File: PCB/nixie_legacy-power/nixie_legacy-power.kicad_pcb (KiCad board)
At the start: 2 copper layers, 33 x 40.6 mm, 23 parts

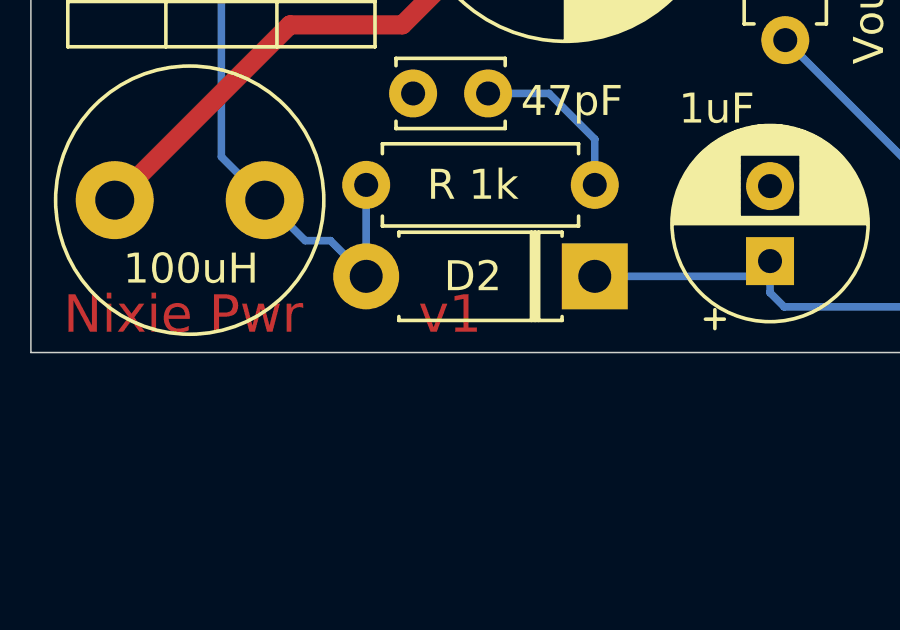
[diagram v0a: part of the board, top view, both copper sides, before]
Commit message: added i2c_rtc_test.c to test interfacing with RX8025 rtc module
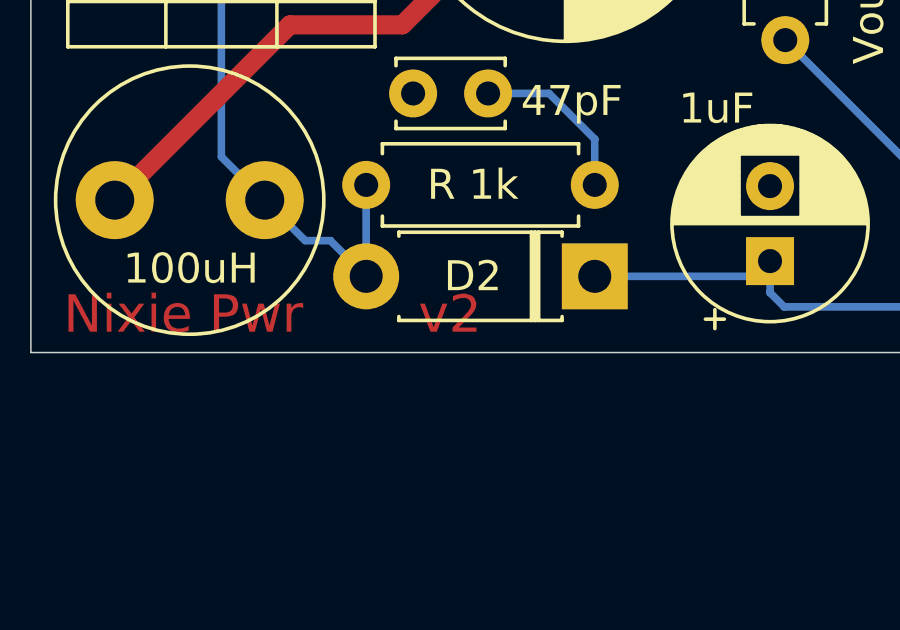
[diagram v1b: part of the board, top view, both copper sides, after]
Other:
- board text added: "WARNING: High Voltage"
- board text added: "v2"
- board text removed: "v1"
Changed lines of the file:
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@@
   (general
     (thickness 1.6)
-    (drawings 14)
+    (drawings 18)
     (tracks 75)
     (zones 0)
@@
   )
   (setup
-    (last_trace_width 0.254)
+    (last_trace_width 0.25)
     (user_trace_width 0.254)
     (user_trace_width 0.635)
@@
     (solder_mask_min_width 0.25)
     (aux_axis_origin 0 0)
-    (visible_elements FFFFFF7F)
+    (visible_elements 7FFFFFFF)
     (pcbplotparams
       (layerselection 0x110f0_ffffffff)
@@
     )
   )
-  (gr_text v1 (at 101.854 116.84) (layer F.Cu)
+  (gr_line (start 99.06 102.362) (end 88.138 102.362) (layer B.SilkS) (width 0.5))
+  (gr_line (start 102.87 98.552) (end 99.06 102.362) (layer B.SilkS) (width 0.5))
+  (gr_line (start 120.65 98.552) (end 102.87 98.552) (layer B.SilkS) (width 0.5))
+  (gr_text "WARNING:\nHigh Voltage" (at 106.934 106.172) (layer B.SilkS)
+    (effects (font (size 1 1) (thickness 0.15)) (justify mirror))
+  )
+  (gr_text v2 (at 101.854 116.84) (layer F.Cu)
     (effects (font (size 1.25 1.25) (thickness 0.2)))
   )

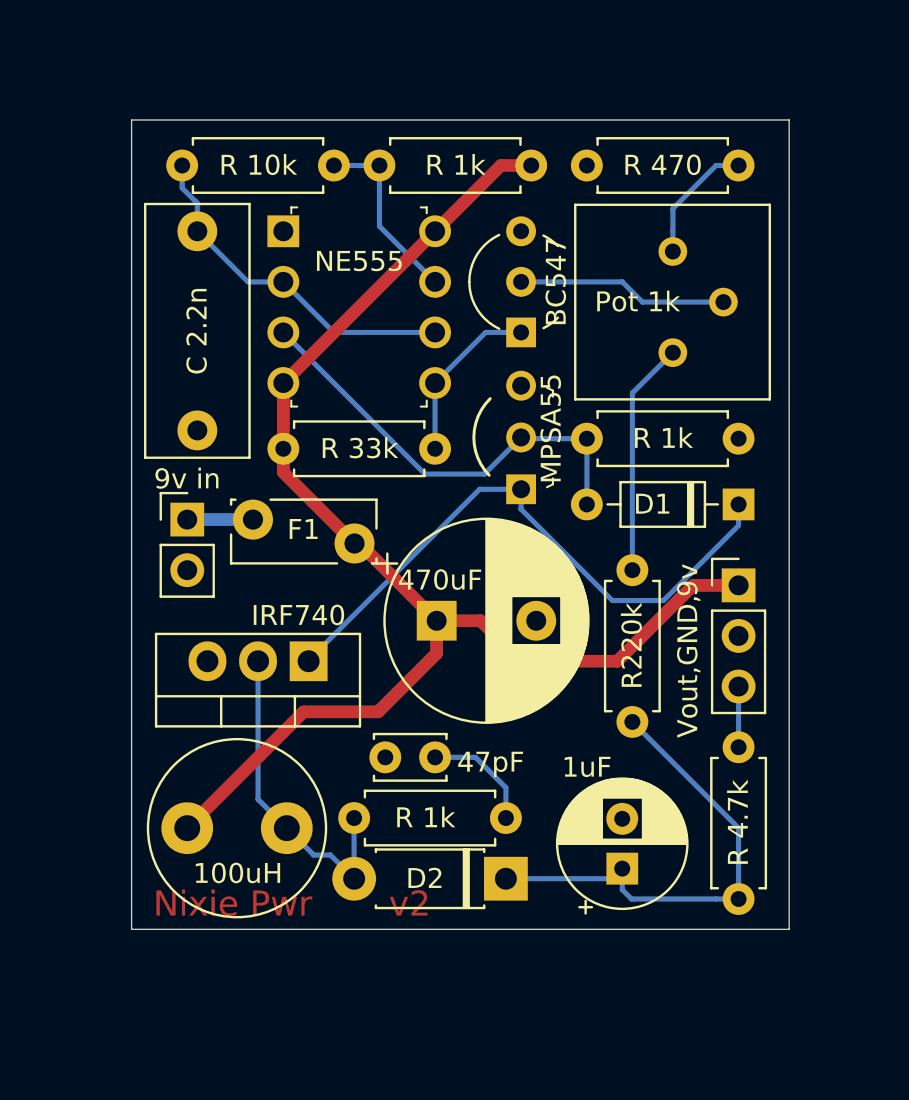
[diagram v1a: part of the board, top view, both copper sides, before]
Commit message: Updating power PCB to v2 to include 5v regulator and support post hole
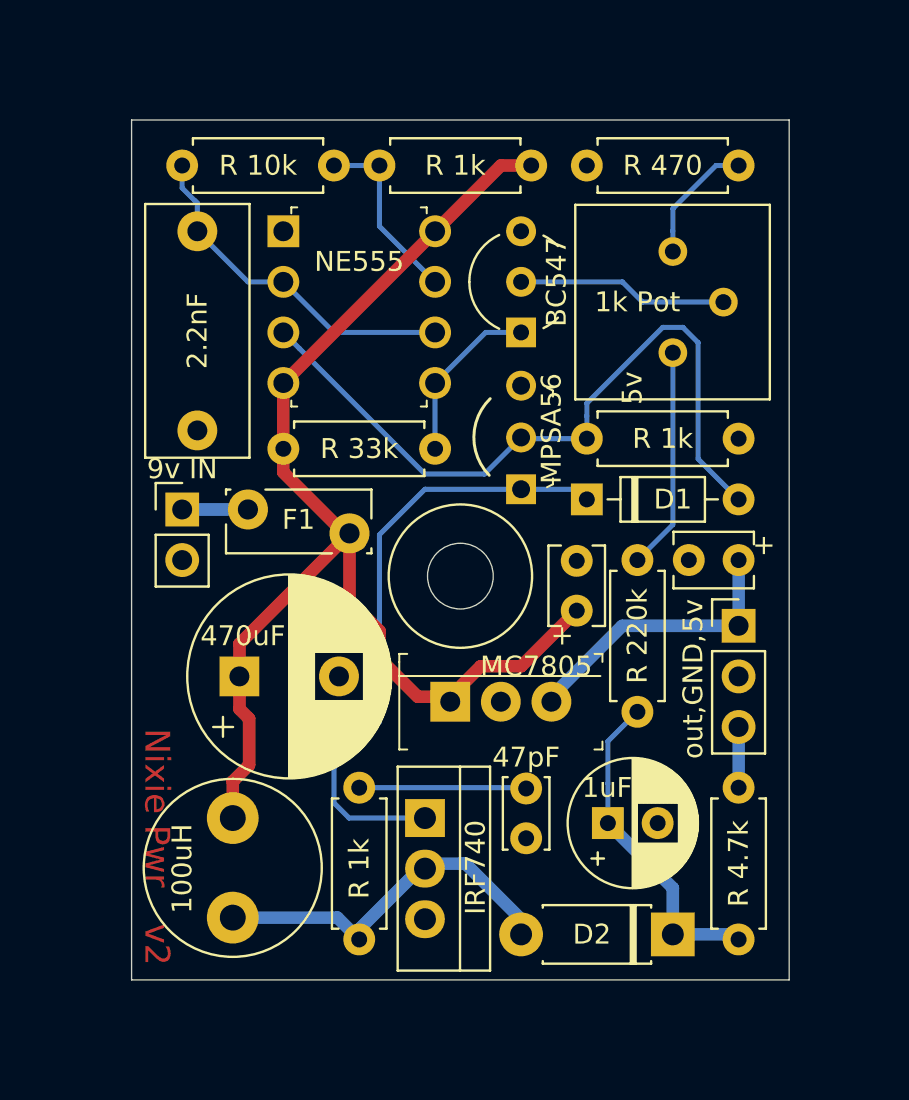
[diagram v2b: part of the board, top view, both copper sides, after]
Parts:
- removed R220k: 220k, Resistor_THT:R_Axial_DIN0207_L6.3mm_D2.5mm_P7.62mm_Horizontal
- added +: 220nTANT, Capacitor_THT:C_Disc_D3.8mm_W2.6mm_P2.50mm, F.Cu at (110.2, 102.1)
- added 5v: 220nTANT, Capacitor_THT:C_Disc_D3.8mm_W2.6mm_P2.50mm, F.Cu at (118.4, 99.6)
- added MC7805: MC7805CT-BP, digikey-footprints:TO-220-3, F.Cu at (103.9, 106.7)
- added R 220k: 220k, Resistor_THT:R_Axial_DIN0207_L6.3mm_D2.5mm_P7.62mm_Horizontal, F.Cu at (113.3, 99.6)
- 1k Pot: renamed from Pot 1k; value R_POT_US -> 1k
- 2.2nF: renamed from C 2.2n
- 9v IN: renamed from 9v in
- R 470: value 47 -> 470
- moved 470uF 10.3 mm to (93.3, 105.4)
- moved IRF740 9.80 mm to (102.6, 112.5), turned to 270 degrees
- moved D2 8.84 mm to (115.1, 118.4)
- moved D1 7.62 mm to (110.7, 96.5), turned to 0 degrees
- moved R 1k 6.10 mm to (99.3, 118.6), turned to 90 degrees
- moved 47pF 4.83 mm to (107.7, 111.0), turned to 270 degrees
- moved 1uF 2.40 mm to (111.8, 112.8), turned to 0 degrees
- moved 100uH 2.34 mm to (93.0, 112.5), turned to 270 degrees
- moved R 4.7k 2.03 mm to (118.4, 111.0)
- moved out,GND, 2.03 mm to (118.4, 102.9)
- moved F1 0.57 mm to (93.7, 97.0)
- moved 9v IN 0.57 mm to (90.4, 97.0)
- renumbered MPSA55 to MPSA56, Vout,GND, to out,GND,
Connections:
- out,GND, pad 1: 9v -> 5v
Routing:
- net Net-(D1-Pad2): track 22.3 -> 36.9 mm
- net 5v: track 0.00 -> 14.2 mm
- net Net-(C4-Pad1): track 24.2 -> 16.5 mm
- net 9v: track 67.6 -> 63.3 mm
- net Net-(C3-Pad1): track 5.71 -> 8.40 mm
- net Net-(D2-Pad2): track 16.5 -> 18.7 mm
- net Net-(R7-Pad1): track 11.8 -> 11.2 mm
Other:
- board size 33 x 40.6 mm -> 33 x 43.2 mm
- board text added: "+"

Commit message: power pcb updated. wrote my name on the silk screen :)
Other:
- board text added: "Gilder 2021"
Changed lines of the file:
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@@
   (general
     (thickness 1.6)
-    (drawings 22)
+    (drawings 23)
     (tracks 93)
     (zones 0)
@@
     )
   )
+  (gr_text "Gilder 2021" (at 89.154 106.426 270) (layer F.SilkS)
+    (effects (font (size 1 1) (thickness 0.15)))
+  )
   (gr_circle (center 104.394 100.374) (end 106.044 100.374) (layer F.Fab) (width 0.0254))

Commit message: power pcb. added input polarity protection diode and rearranged board to fit accordingly. removed ground plane from high voltage zone. (recommit)
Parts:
- added D->: D, Diode_THT:D_DO-41_SOD81_P2.54mm_Vertical_KathodeUp, F.Cu at (94.5, 96.3)
- 9v+: renamed from 9v IN
- C 2n2: renamed from 2.2nF
- R 4k7: renamed from R 4.7k
- moved R 33k 23.0 mm to (118.4, 96.5), turned to 180 degrees
- moved D1 14.3 mm to (96.8, 93.5)
- moved BC547 5.68 mm to (106.4, 82.5), turned to 270 degrees
- moved F1 5.68 mm to (99.3, 96.0), turned to 270 degrees
- moved 470uF 2.42 mm to (90.9, 105.9)
- moved MPSA56 1.55 mm to (107.7, 94.5)
- moved 100uH 0.76 mm to (93.0, 113.3)
- moved R 220k 0.76 mm to (113.3, 100.3)
- moved 9v+ 0.36 mm to (90.2, 96.8)
- moved + 0.26 mm to (110.0, 102.1)
- renumbered 1uF to C4, out,GND, to Out,GND,
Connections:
- 9v+ pad 1: Net-(F1-Pad1) -> Net-(D3-Pad2)
- F1 pad 1: Net-(F1-Pad1) -> Net-(D3-Pad1)
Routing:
- net GND: track 0.00 -> 62.8 mm
- net Net-(D1-Pad2): track 36.9 -> 18.8 mm
- net 9v: track 63.3 -> 78.9 mm
- net Net-(Q1-Pad1): track 8.67 -> 24.1 mm
- net Net-(D1-Pad1): track 31.0 -> 40.9 mm
- net Net-(D3-Pad2): track 0.00 -> 5.16 mm
- net Net-(D3-Pad1): track 0.00 -> 4.93 mm
- net Net-(F1-Pad1): track 3.30 -> 0.00 mm
- net Net-(Q1-Pad2): track 10.6 -> 11.8 mm
- net Net-(D2-Pad2): track 18.7 -> 17.9 mm

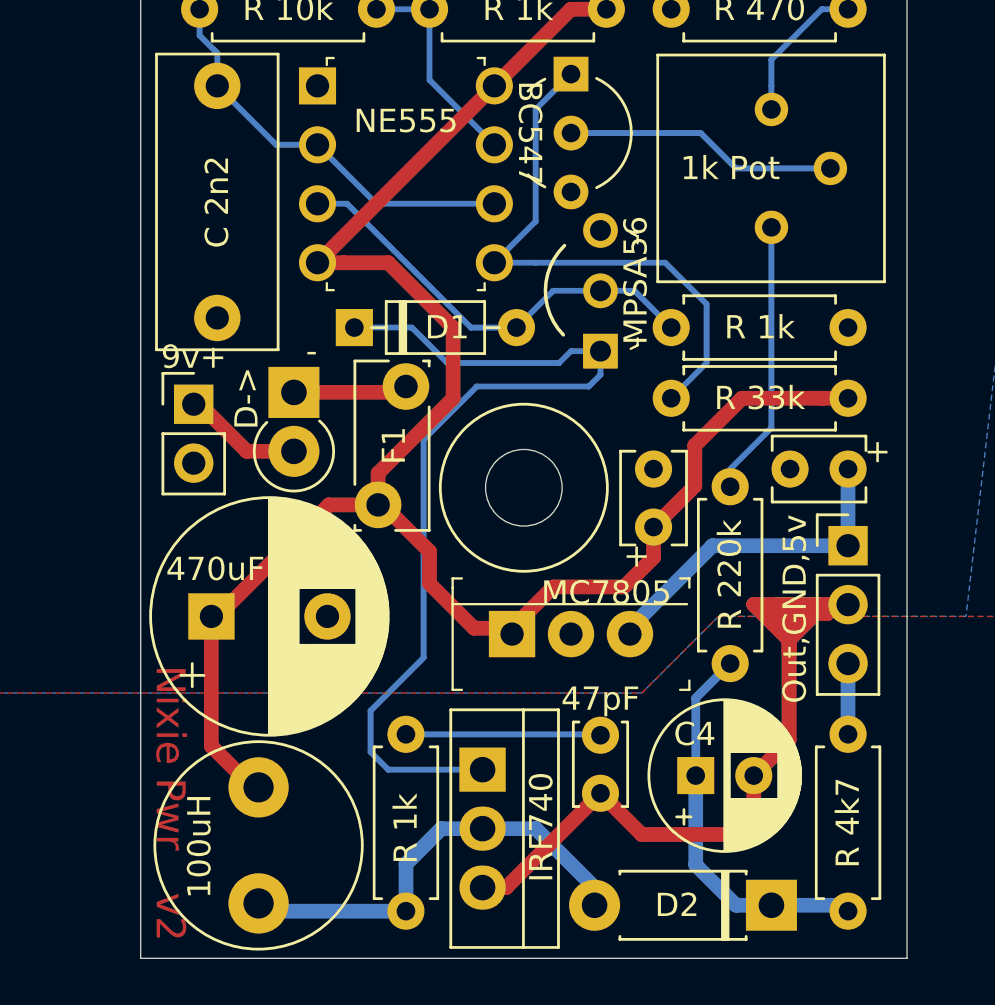
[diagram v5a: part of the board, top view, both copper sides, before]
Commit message: -power board: updated 7805 footprint to better fit piece, "A55" instead of "A56", 9v input pad shape swap so that ground makes sense -digit board: added resistor value, vertical connector, correct pinout for rear mounting to match header population on demux board -new_rtc_pcbHack: deprecated. works with v1 of digit boards (with bad header pinout) but no longer needed. did not update with time demux, only displayed idle animation and set menu
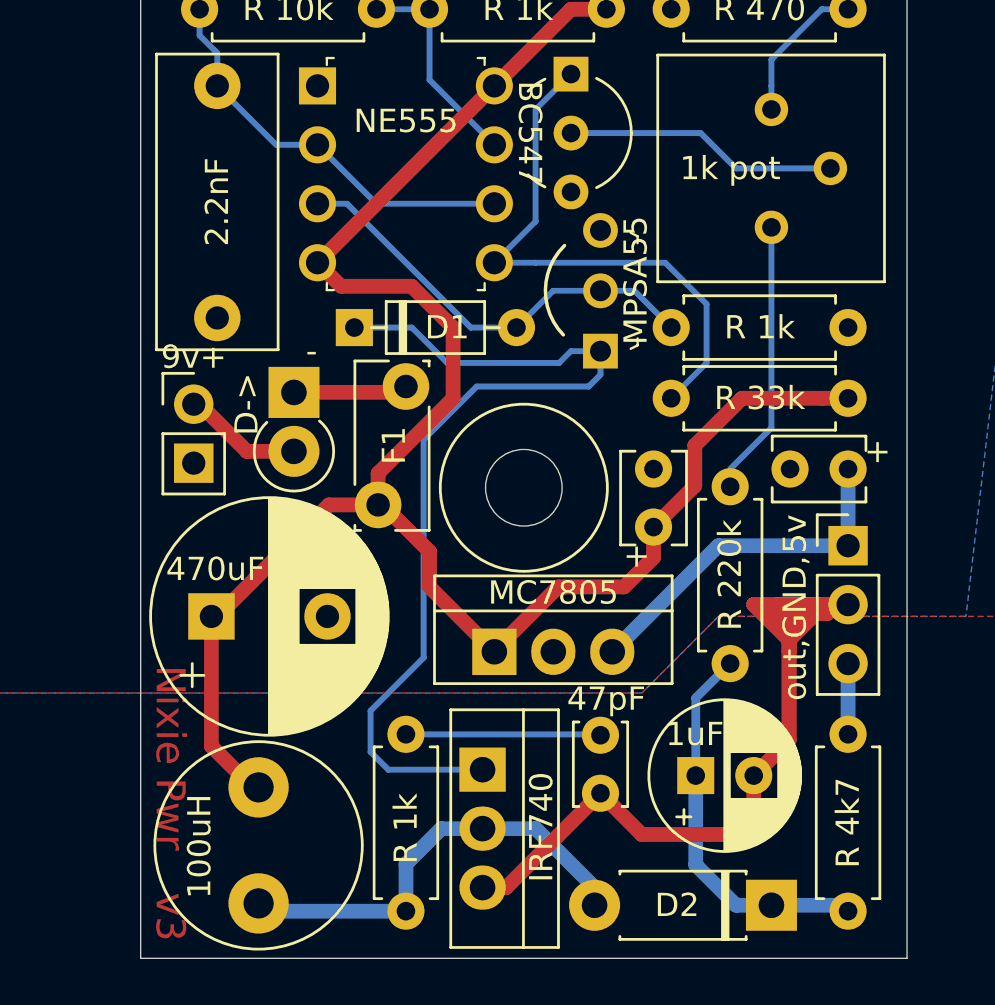
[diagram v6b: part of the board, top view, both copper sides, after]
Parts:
- removed MPSA56: MPSA56-AP, digikey-footprints:TO-92-3_Formed_Leads
- added MPSA55: MPSA55-AP, digikey-footprints:TO-92-3_Formed_Leads, F.Cu at (107.7, 94.5)
- 1k pot: renamed from 1k Pot
- 2.2nF: renamed from C 2n2
- MC7805: footprint digikey-footprints:TO-220-3 -> Package_TO_SOT_THT:TO-220-3_Vertical
- moved MC7805 1.08 mm to (103.1, 107.4)
- renumbered C4 to 1uF, Out,GND, to out,GND,
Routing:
- net 5v: track 14.2 -> 15.4 mm
- net 9v: track 78.9 -> 79.6 mm
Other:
- board text added: "v3"
- board text removed: "v2"
